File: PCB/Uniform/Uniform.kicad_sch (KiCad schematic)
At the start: 156 parts, among them U1 STM32L072KZT6

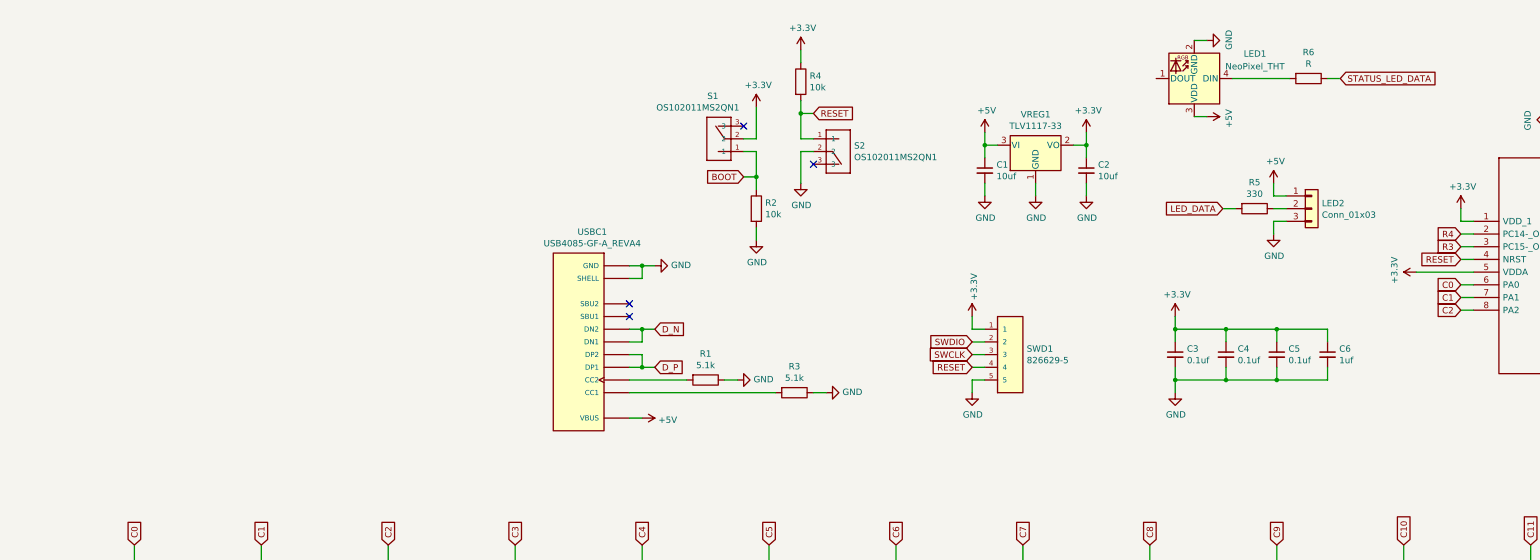
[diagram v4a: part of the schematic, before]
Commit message: Added 2 more Neopixels and supporting logic level shifter
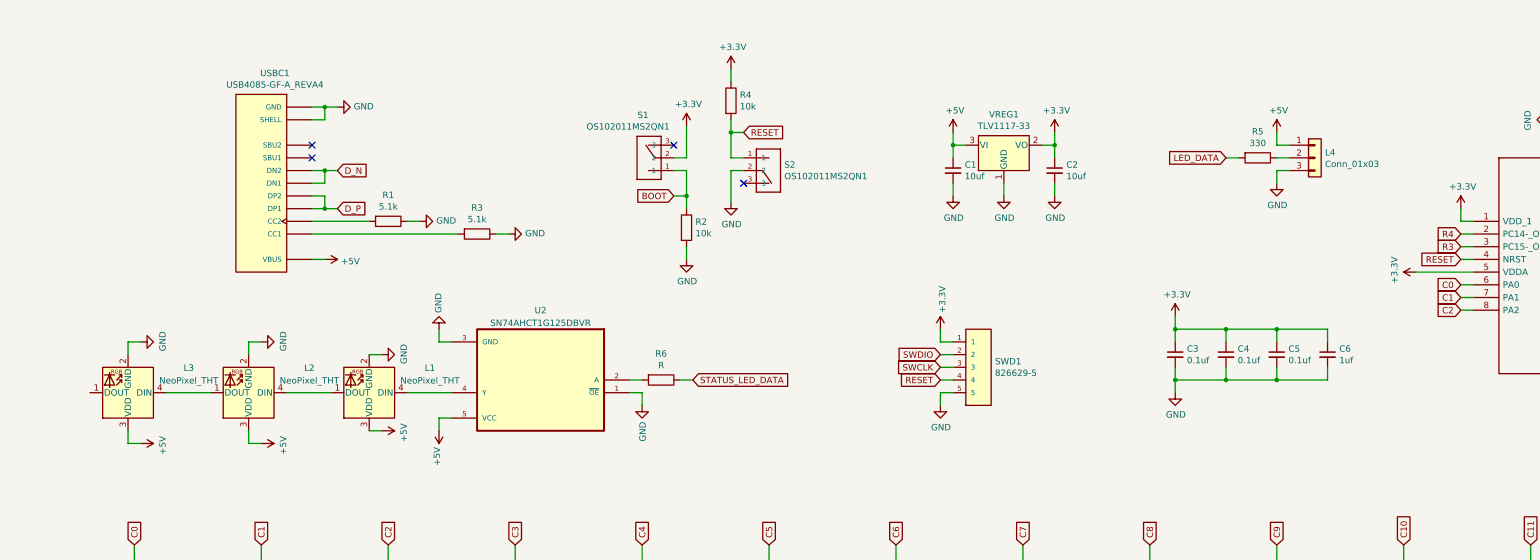
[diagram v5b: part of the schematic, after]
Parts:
- added L2, L3: NeoPixel_THT, Neopixel:LED_D5.0mm-4_RGB, symbol LED:NeoPixel_THT
- added U2: SN74AHCT1G125DBVR, SN74AHCT1G125DBVR:SOT95P280X145-5N, symbol SN74AHCT1G125DBVR:SN74AHCT1G125DBVR
- R1, R2, R3, R4: footprint Resistor_THT:R_Axial_DIN0309_L9.0mm_D3.2mm_P12.70mm_Horizontal -> Resistor_THT:R_Axial_DIN0204_L3.6mm_D1.6mm_P7.62mm_Horizontal
- renumbered LED1 to L1, LED2 to L4
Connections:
- net +5V: now also L2.3 (VDD), L3.3 (VDD), U2.5 (VCC)
- net GND: now also L2.2 (GND), L3.2 (GND), U2.1 (~{OE}), U2.3 (GND)
- net at R6.2: now also U2.2 (A); no longer L1.4 (DIN)
- net at L1.1 (DOUT): now also L2.4 (DIN)
- new net: L1.4 (DIN), U2.4 (Y)
- new net: L2.1 (DOUT), L3.4 (DIN)
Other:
- moved on the sheet: C1, C2, L1, L4, R1, R2, R3, R4, R5, R6, S1, S2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

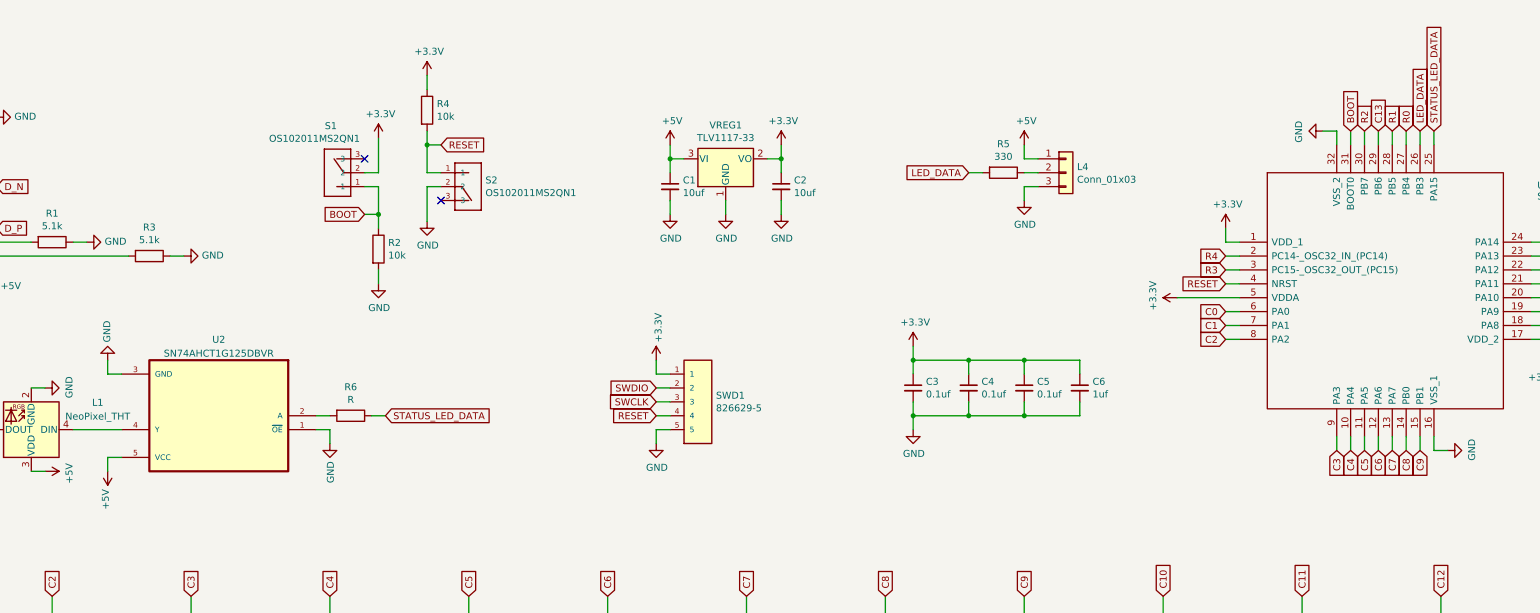
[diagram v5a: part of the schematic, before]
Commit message: Move status LED resistor between the logic level shifter and the LED to fix flicker issue
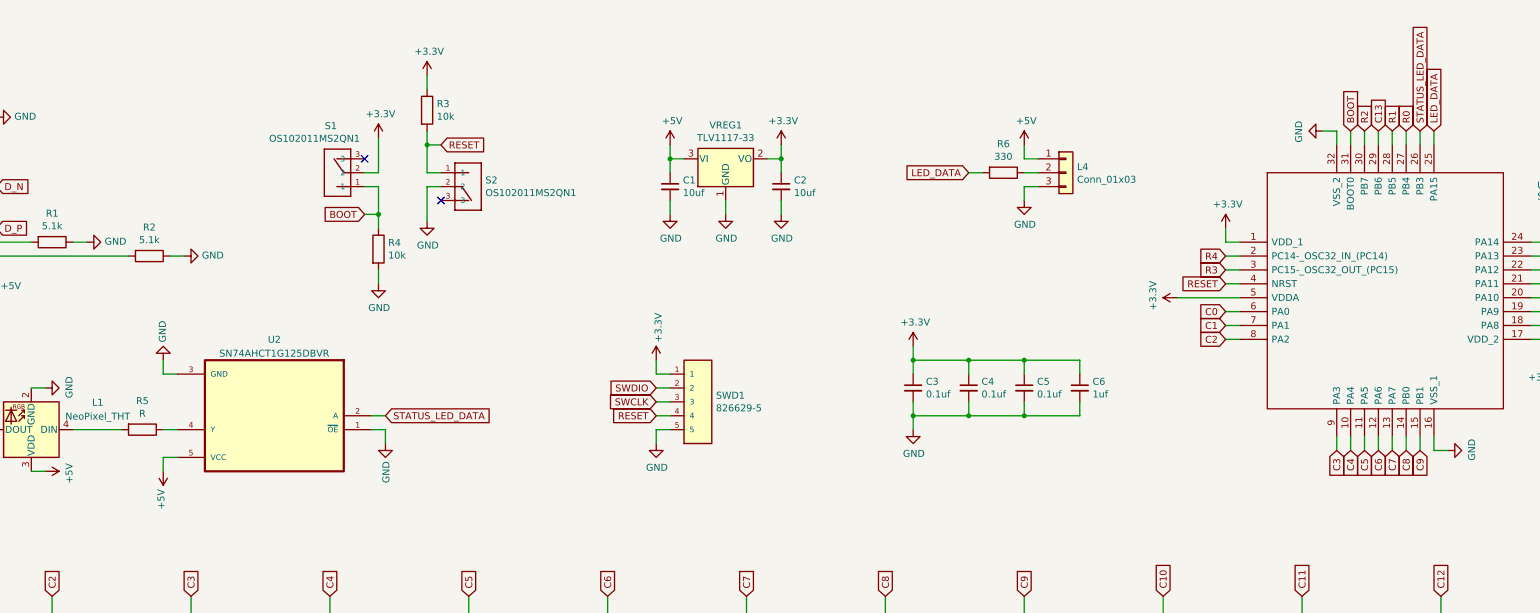
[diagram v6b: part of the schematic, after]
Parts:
- renumbered R3 to R2, R4 to R3, R2 to R4, R6 to R5, R5 to R6
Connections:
- net LED_DATA: now also U1.25 (PA15); no longer U1.26 (PB3)
- net STATUS_LED_DATA: now also U1.26 (PB3), U2.2 (A); no longer R5.1, U1.25 (PA15)
- net at R5.2: now also L1.4 (DIN); no longer U2.2 (A)
- net at U2.4 (Y): now also R5.1; no longer L1.4 (DIN)
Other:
- moved on the sheet: R5, U2
